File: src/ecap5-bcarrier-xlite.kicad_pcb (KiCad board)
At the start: 4 copper layers, 160.8 x 54.7 mm, 55 parts, among them J1 DDR4_SODIMM_Board, J2 DDR4_SODIMM_Board, J3 Conn_01x04, J4 Conn_01x04, J5 USB_C_Receptacle_USB2.0_14P, J6 Conn_Coaxial, J7 Conn_Coaxial, J8 Conn_Coaxial, J9 1935161, Q1 BC846BR13, Q2 BC846BR13, SW1 RESET_SOM1, SW2 RESET_SOM2, SW3 USER1, SW4 USER1, U1 FT232RN, U2 AP7375-33SA-7

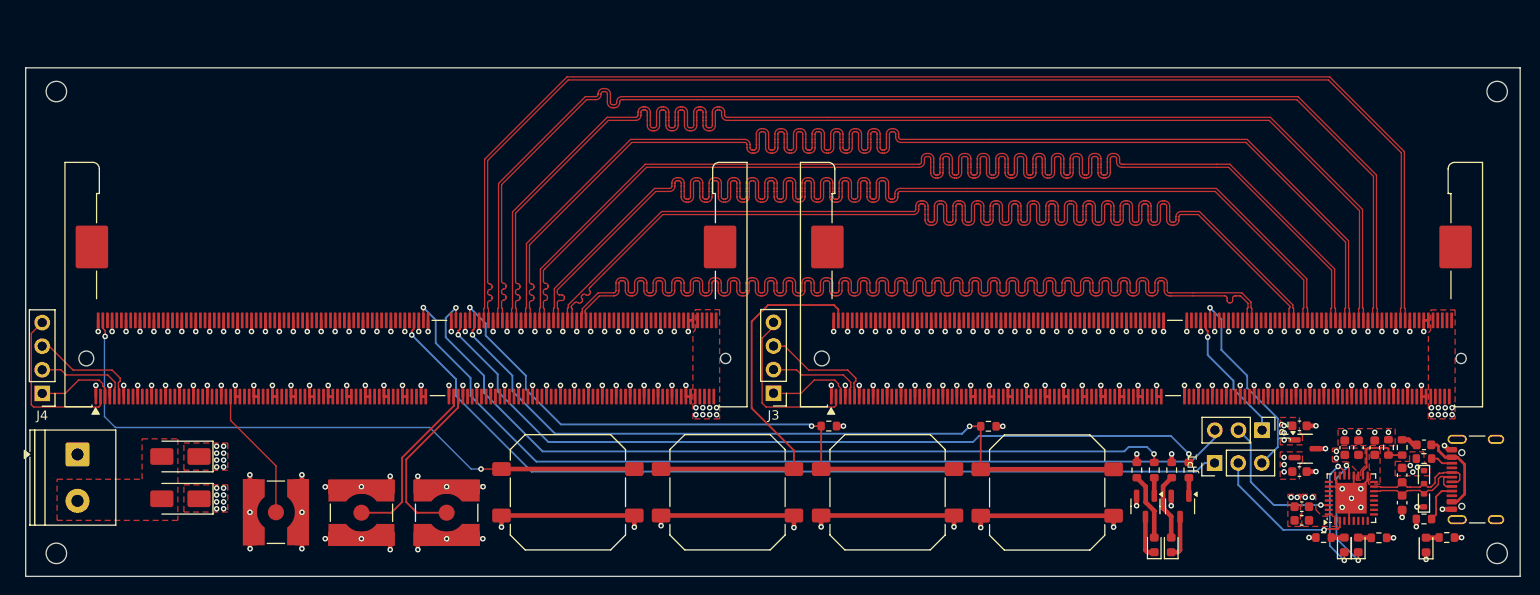
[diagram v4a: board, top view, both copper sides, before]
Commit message: Finish routing the single-ended signals
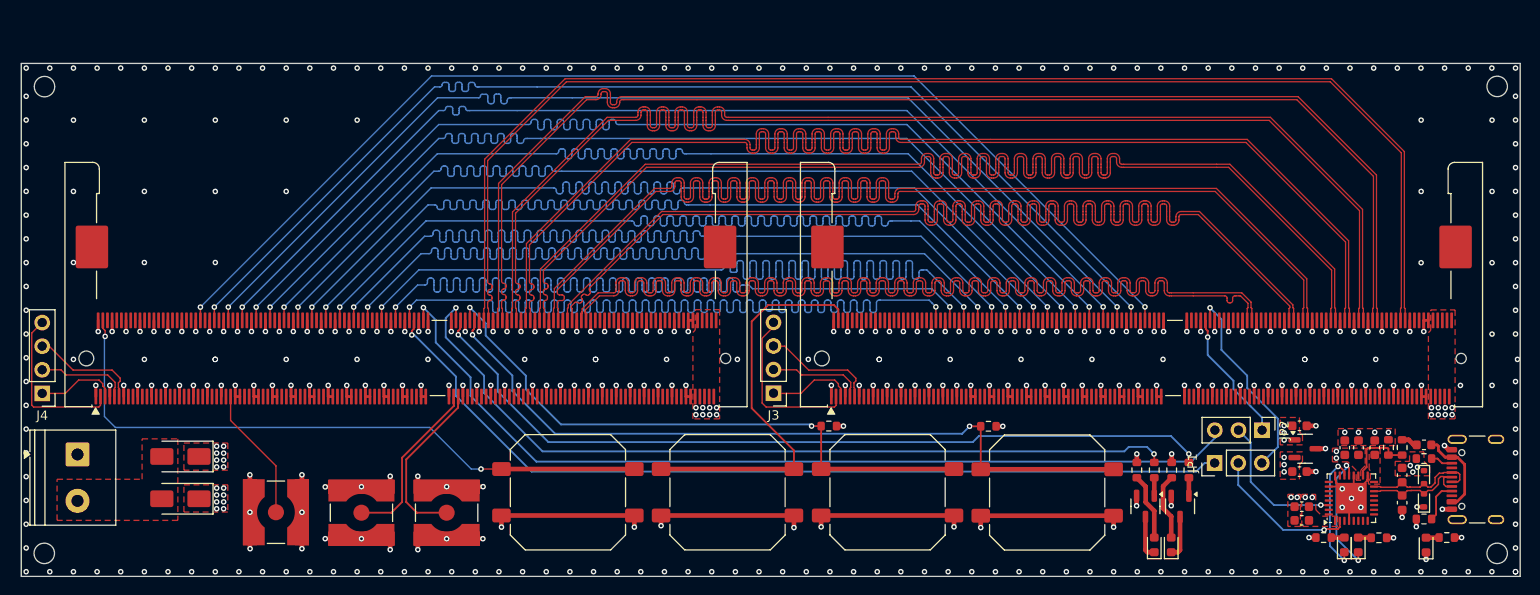
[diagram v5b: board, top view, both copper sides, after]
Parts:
- moved H1 1.38 mm to (33.5, 65.5)
- moved H4 1.30 mm to (33.4, 115.7)
- moved H2 0.55 mm to (189.8, 65.5)
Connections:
- J1 pad 100: unconnected-(J1-Pad100) -> /SOM1/SE31
- J1 pad 106: unconnected-(J1-Pad106) -> /SOM1/SE33
- J1 pad 112: unconnected-(J1-Pad112) -> /SOM1/SE35
- J1 pad 118: unconnected-(J1-Pad118) -> /SOM1/SE37
- J1 pad 124: unconnected-(J1-Pad124) -> /SOM1/SE39
- J1 pad 130: unconnected-(J1-Pad130) -> /SOM1/SE41
- J1 pad 136: unconnected-(J1-Pad136) -> /SOM1/SE43
- J1 pad 46: unconnected-(J1-Pad46) -> /SOM1/SE13
- J1 pad 52: unconnected-(J1-Pad52) -> /SOM1/SE15
- J1 pad 58: unconnected-(J1-Pad58) -> /SOM1/SE17
- J1 pad 64: unconnected-(J1-Pad64) -> /SOM1/SE19
- J1 pad 70: unconnected-(J1-Pad70) -> /SOM1/SE21
- J1 pad 76: unconnected-(J1-Pad76) -> /SOM1/SE23
- J1 pad 82: unconnected-(J1-Pad82) -> /SOM1/SE25
- J1 pad 88: unconnected-(J1-Pad88) -> /SOM1/SE27
- J1 pad 94: unconnected-(J1-Pad94) -> /SOM1/SE29
- J2 pad 100: unconnected-(J2-Pad100) -> /SOM1/SE25
- J2 pad 106: unconnected-(J2-Pad106) -> /SOM1/SE23
- J2 pad 112: unconnected-(J2-Pad112) -> /SOM1/SE21
- J2 pad 118: unconnected-(J2-Pad118) -> /SOM1/SE19
- J2 pad 124: unconnected-(J2-Pad124) -> /SOM1/SE17
- J2 pad 130: unconnected-(J2-Pad130) -> /SOM1/SE15
- J2 pad 136: unconnected-(J2-Pad136) -> /SOM1/SE13
- J2 pad 46: unconnected-(J2-Pad46) -> /SOM1/SE43
- J2 pad 52: unconnected-(J2-Pad52) -> /SOM1/SE41
- J2 pad 58: unconnected-(J2-Pad58) -> /SOM1/SE39
- J2 pad 64: unconnected-(J2-Pad64) -> /SOM1/SE37
- J2 pad 70: unconnected-(J2-Pad70) -> /SOM1/SE35
- J2 pad 76: unconnected-(J2-Pad76) -> /SOM1/SE33
- J2 pad 82: unconnected-(J2-Pad82) -> /SOM1/SE31
- J2 pad 88: unconnected-(J2-Pad88) -> /SOM1/SE29
- J2 pad 94: unconnected-(J2-Pad94) -> /SOM1/SE27
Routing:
- net /SOM1/SE13: track 0.00 -> 125.1 mm, vias 0 -> 2
- net /SOM1/SE15: track 0.00 -> 124.6 mm, vias 0 -> 2
- net /SOM1/SE43: track 0.00 -> 123.8 mm, vias 0 -> 2
- net /SOM1/SE41: track 0.00 -> 123.7 mm, vias 0 -> 2
- net /SOM1/SE17: track 0.00 -> 120.1 mm, vias 0 -> 2
- net /SOM1/SE39: track 0.00 -> 119.6 mm, vias 0 -> 2
- net /SOM1/SE21: track 0.00 -> 119.5 mm, vias 0 -> 2
- net /SOM1/SE35: track 0.00 -> 118.9 mm, vias 0 -> 2
- net /SOM1/SE25: track 0.00 -> 115.4 mm, vias 0 -> 2
- net /SOM1/SE31: track 0.00 -> 115.0 mm, vias 0 -> 2
- net /SOM1/SE19: track 0.00 -> 114.9 mm, vias 0 -> 2
- net /SOM1/SE23: track 0.00 -> 114.0 mm, vias 0 -> 2
- net /SOM1/SE37: track 0.00 -> 114.0 mm, vias 0 -> 2
- net /SOM1/SE33: track 0.00 -> 113.4 mm, vias 0 -> 2
- net /SOM1/SE27: track 0.00 -> 109.8 mm, vias 0 -> 2
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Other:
- board size 160.8 x 54.7 mm -> 161.3 x 55.2 mm

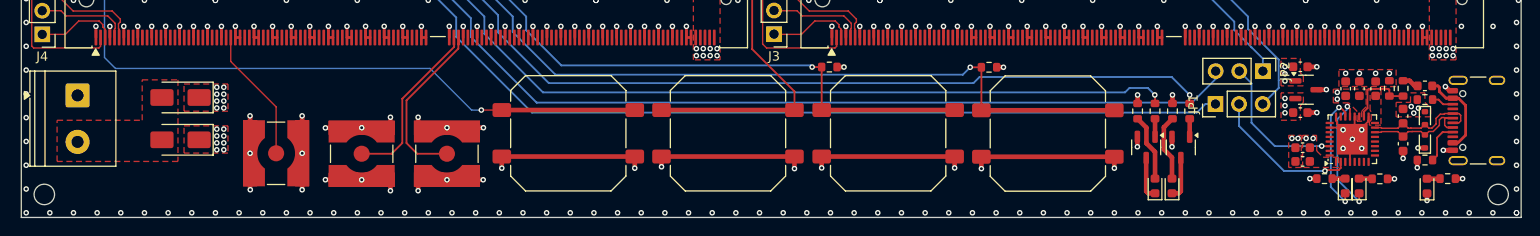
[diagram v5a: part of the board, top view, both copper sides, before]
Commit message: Start adding silkscreen
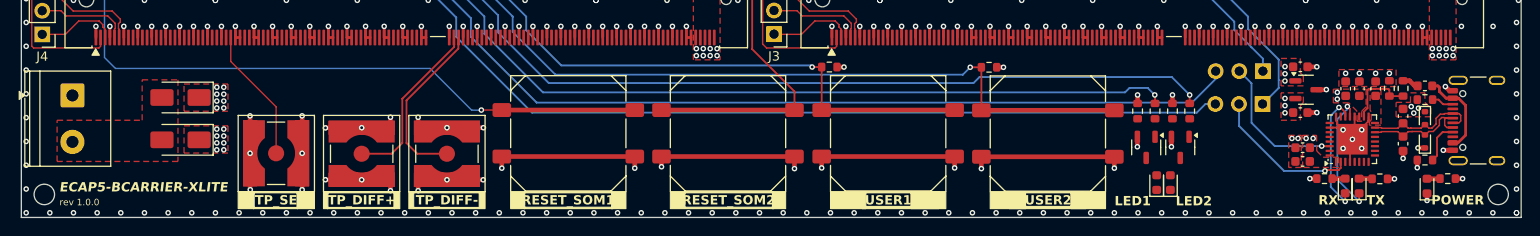
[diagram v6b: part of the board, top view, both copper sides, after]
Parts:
- moved JP1 5.07 mm to (164.4, 106.0), turned to -90 degrees
- moved J9 0.55 mm to (36.5, 105.1)
- moved D2 0.40 mm to (153.1, 114.5)
- moved D8 0.40 mm to (154.5, 114.5)
- moved Q2 0.06 mm to (155.6, 110.7)
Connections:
- JP1 pad 1: /SOM1.UART_RX -> /SOM2.UART_RX
- JP1 pad 3: /SOM2.UART_RX -> /SOM1.UART_RX
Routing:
- net Net-(D2-A): track 7.21 -> 0.00 mm
- net Net-(D8-A): track 7.19 -> 0.00 mm
- net Net-(D8-K): track 4.62 -> 0.00 mm
- net Net-(D2-K): track 4.62 -> 0.00 mm
- net Net-(Q2-B): track 1.94 -> 0.00 mm
- net Net-(Q1-B): track 1.94 -> 0.00 mm
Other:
- board text added: "ECAP5-BCARRIER-XLITE"
- board text added: "LED1"
- board text added: "LED2"
- board text added: "POWER"
- board text added: "RESET_SOM1"
- board text added: "RESET_SOM2"
- board text added: "RX"
- board text added: "TP_DIFF+"
- board text added: "TP_DIFF-"
- board text added: "TP_SE"
- board text added: "TX"
- board text added: "USER1"
- board text added: "USER2"
- board text added: "rev 1.0.0"

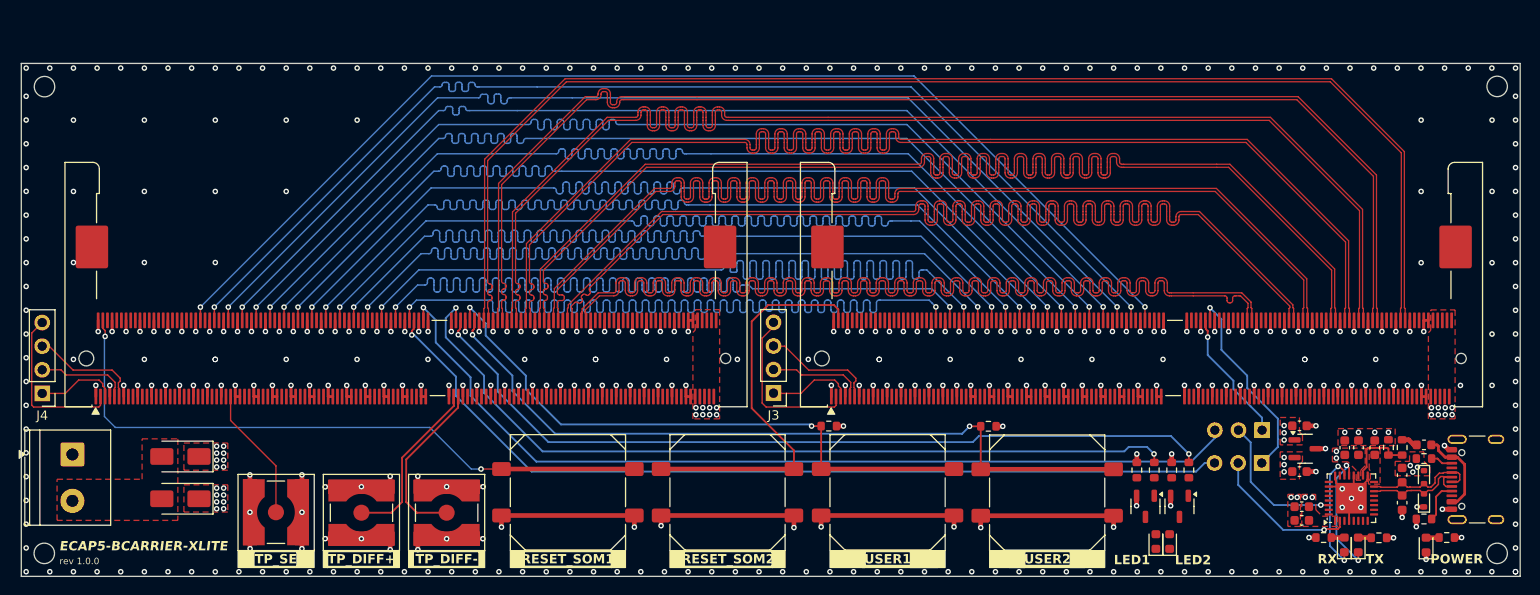
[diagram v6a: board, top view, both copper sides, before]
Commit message: Add silkscreen
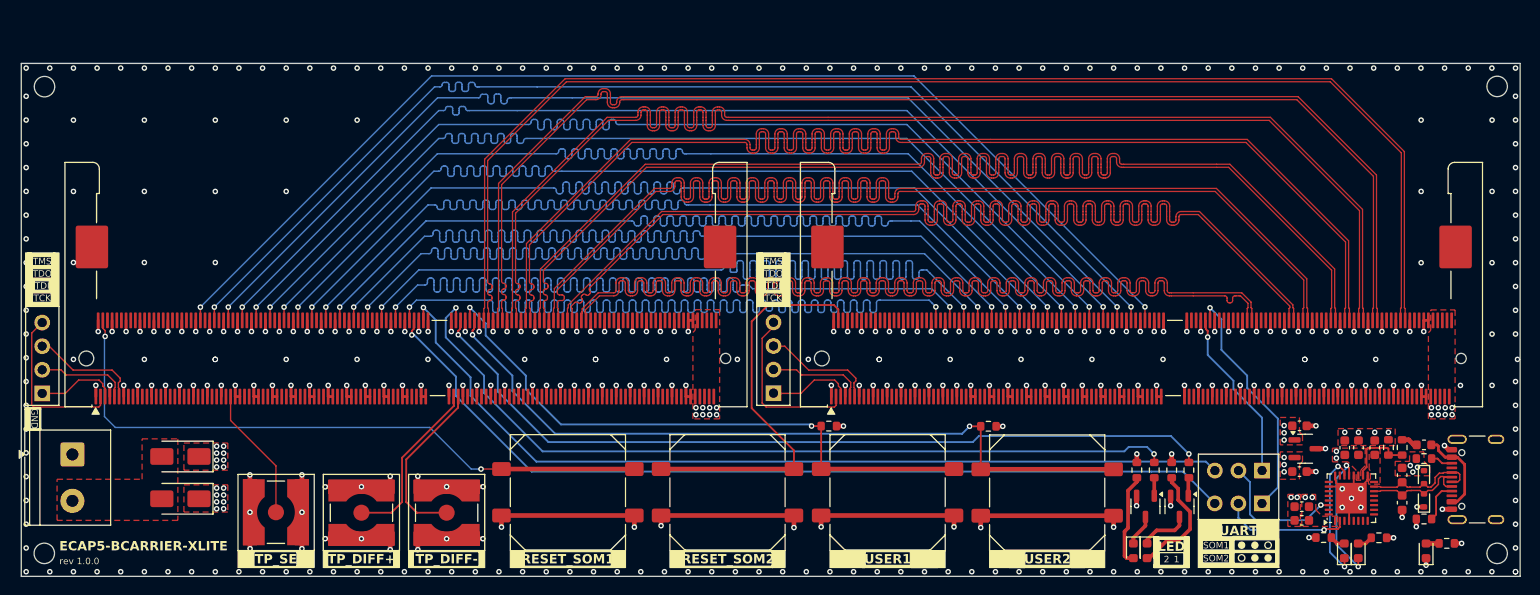
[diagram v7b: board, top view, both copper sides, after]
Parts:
- moved JP1 4.35 mm to (164.5, 110.3)
- moved JP2 4.35 mm to (164.5, 106.8)
- moved D2 2.62 mm to (150.6, 115.5), turned to -90 degrees
- moved D8 2.62 mm to (152.1, 115.5), turned to -90 degrees
- moved D6 0.64 mm to (173.3, 115.5)
- moved D7 0.64 mm to (174.8, 115.5)
- moved D5 0.62 mm to (182.1, 115.5)
- moved R5 0.62 mm to (184.3, 114.7)
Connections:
- J1 pad 148: /LED1 -> /LED2
- J1 pad 150: /LED2 -> /LED1
- R11 pad 2: /LED2 -> /LED1
- R9 pad 2: /LED1 -> /LED2
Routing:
- net Net-(D8-A): track 0.00 -> 12.3 mm
- net Net-(D2-A): track 0.00 -> 10.0 mm
- net Net-(D8-K): track 0.00 -> 5.45 mm
- net /SOM2.UART_TX: track 14.3 -> 18.7 mm
- net /SOM2.UART_RX: track 21.8 -> 26.1 mm
- net Net-(D2-K): track 0.00 -> 3.40 mm
- net /UART.RX: track 16.1 -> 13.8 mm
- net /SOM1.UART_TX: track 98.4 -> 96.4 mm
- net Net-(Q2-B): track 0.00 -> 1.96 mm
- net Net-(Q1-B): track 0.00 -> 1.94 mm
- net /SOM1.UART_RX: track 95.8 -> 96.8 mm
- net /UART.TX: track 15.5 -> 14.6 mm
- net /UART.~{RXLED}: track 13.3 -> 14.1 mm
- net /UART.~{TXLED}: track 13.7 -> 14.4 mm
- net /LED2: track 88.1 -> 88.8 mm
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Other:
- board text added: "1"
- board text added: "2"
- board text added: "GND"
- board text added: "LED"
- board text added: "SOM1"
- board text added: "SOM2"
- board text added: "TCK"
- board text added: "TDI"
- board text added: "TDO"
- board text added: "TMS"
- board text added: "UART"
- board text removed: "LED1"
- board text removed: "LED2"
- board text removed: "POWER"
- board text removed: "RX"
- board text removed: "TX"

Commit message: Fix erc issues
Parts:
- moved J9 0.38 mm to (36.8, 105.1)
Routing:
- net GND: vias 433 -> 427
